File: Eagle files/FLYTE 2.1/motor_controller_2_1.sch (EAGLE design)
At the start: 32 parts, among them J1 XT60-M, U1 MIC29302WU-TRTO-263-5_MCH-M

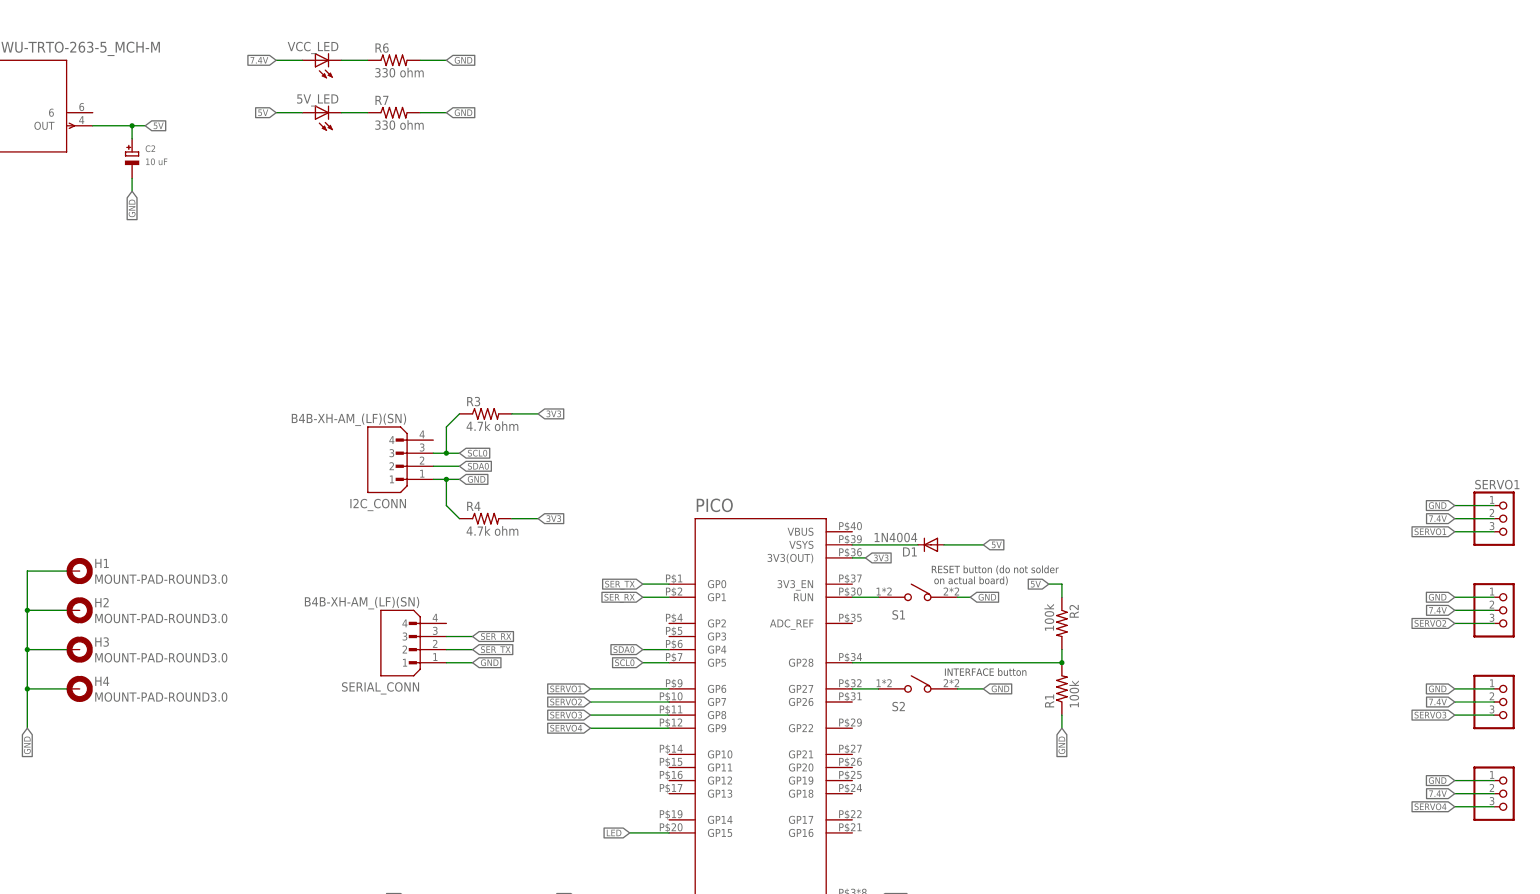
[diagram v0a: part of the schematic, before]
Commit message: Schematics of FC and motor controller
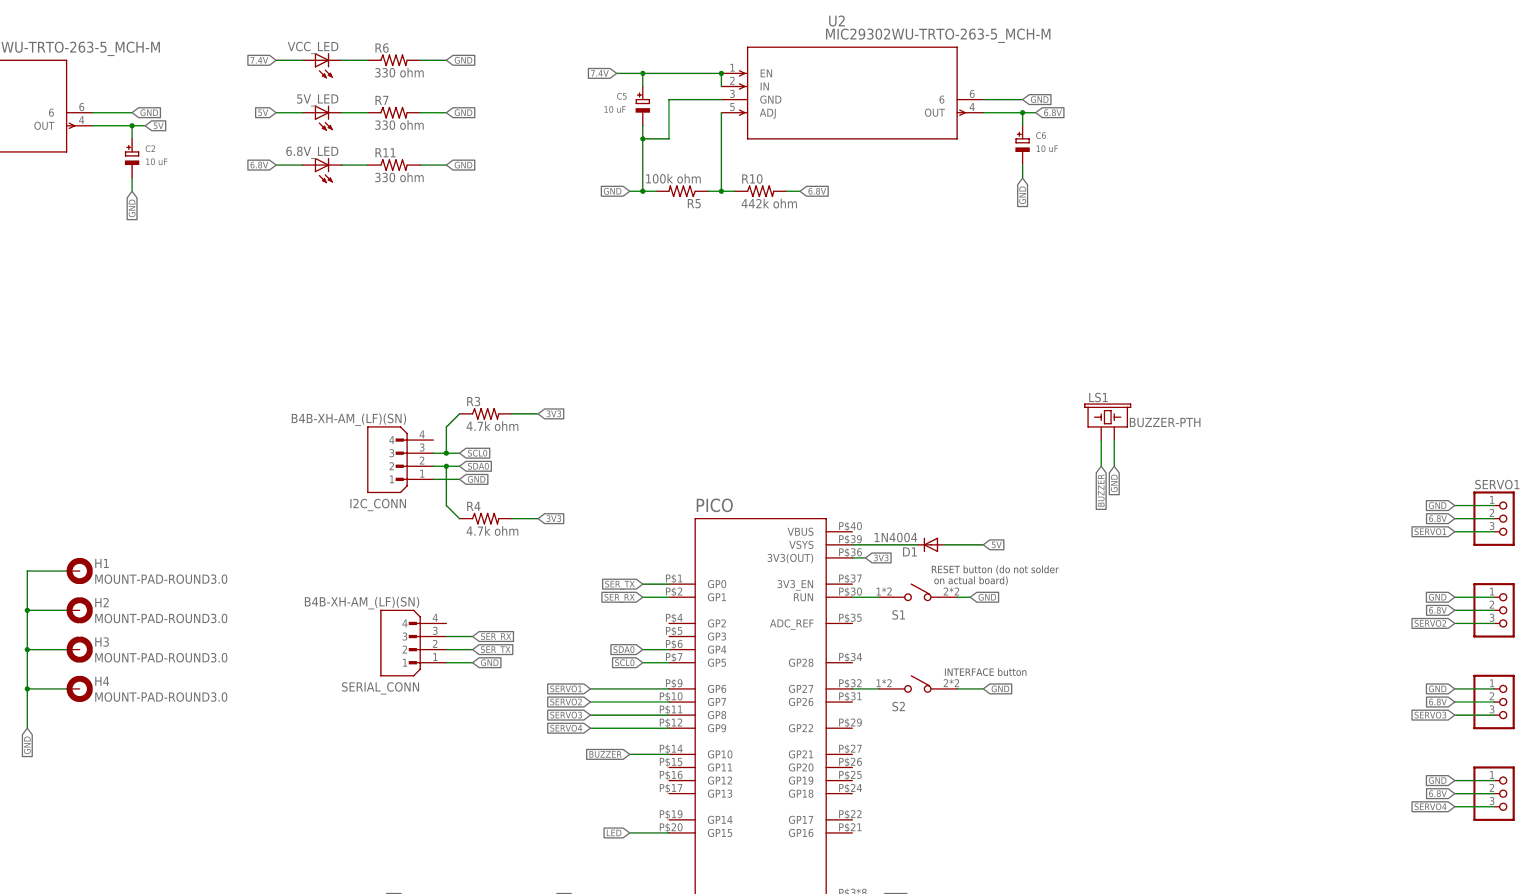
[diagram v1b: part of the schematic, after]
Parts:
- removed R1, R2: 100k, rcl:R-US_R0805
- added 6.8V_LED: (no value), adafruit:LEDCHIPLED_1206
- added C5, C6: 10 uF, microbuilder:CAP_TANTALUMA/3216_WAVE
- added LS1: BUZZER-PTH, SparkFun-Electromechanical:BUZZER-PTH
- added R10: 442k ohm, rcl:R-US_R0805
- added R11: 330 ohm, rcl:R-US_R0805
- added R5: 100k ohm, rcl:R-US_R0805
- added U2: MIC29302WU-TRTO-263-5_MCH-M, MIC29302WU:MIC29302WU-TRTO-263-5_MCH-M
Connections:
- removed net N$4: PICO.GP28, R1.2, R2.2
- new net 6.8V: 6.8V_LED.A, C6.+, R10.2, SERVO1.2, SERVO2.2, SERVO3.2, SERVO4.2, U2.OUT
- new net BUZZER: LS1.1, PICO.GP10
- new net N$5: R10.1, R5.1, U2.ADJ
- new net N$8: 6.8V_LED.C, R11.1
- net 5V: no longer R2.1
- net 7.4V: now also C5.+, U2.EN, U2.IN; no longer SERVO1.2, SERVO2.2, SERVO3.2, SERVO4.2
- net GND: now also C5.-, C6.-, LS1.2, R11.2, R5.2, U1.6, U2.6, U2.GND; no longer R1.1, R4.1
- net SDA0: now also R4.1

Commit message: motor controller v2.1
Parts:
- removed SERVO1, SERVO2, SERVO3, SERVO4: (no value), pinhead:PINHD-1X3
- added J2, J3, J4, J5: S3B-XH-A(LF)(SN), S3B-XH-A_LF__SN_:S3B-XH-A(LF)(SN)
- renumbered S1 to RESET, S2 to INTERFACE
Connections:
- net 6.8V: now also J2.2, J3.2, J4.2, J5.2; no longer SERVO1.2, SERVO2.2, SERVO3.2, SERVO4.2
- net GND: now also J2.1, J3.1, J4.1, J5.1; no longer SERVO1.1, SERVO2.1, SERVO3.1, SERVO4.1
- net SERVO1: now also J2.3; no longer SERVO1.3
- net SERVO2: now also J3.3; no longer SERVO2.3
- net SERVO3: now also J4.3; no longer SERVO3.3
- net SERVO4: now also J5.3; no longer SERVO4.3
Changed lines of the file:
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@@
 <part name="PICO" library="RpiPico" deviceset="RASPBERRY_PICO-NO_DEBUG" device="" override_package3d_urn="urn:adsk.eagle:package:43007819/2" override_package_urn="urn:adsk.eagle:footprint:43007820/1"/>
 <part name="D1" library="adafruit" deviceset="1N4004" device="" override_package3d_urn="urn:adsk.eagle:package:43007855/2" override_package_urn="urn:adsk.eagle:footprint:43007856/1"/>
-<part name="SERVO1" library="pinhead" library_urn="urn:adsk.eagle:library:325" deviceset="PINHD-1X3" device="" package3d_urn="urn:adsk.eagle:package:22458/2"/>
-<part name="SERVO2" library="pinhead" library_urn="urn:adsk.eagle:library:325" deviceset="PINHD-1X3" device="" package3d_urn="urn:adsk.eagle:package:22458/2"/>
-<part name="SERVO3" library="pinhead" library_urn="urn:adsk.eagle:library:325" deviceset="PINHD-1X3" device="" package3d_urn="urn:adsk.eagle:package:22458/2"/>
-<part name="SERVO4" library="pinhead" library_urn="urn:adsk.eagle:library:325" deviceset="PINHD-1X3" device="" package3d_urn="urn:adsk.eagle:package:22458/2"/>
 <part name="H1" library="holes" library_urn="urn:adsk.eagle:library:237" deviceset="MOUNT-PAD-ROUND" device="3.0" package3d_urn="urn:adsk.eagle:package:14280/1" override_package3d_urn="urn:adsk.eagle:package:43007850/2" override_package_urn="urn:adsk.eagle:footprint:14251/1"/>
 <part name="H2" library="holes" library_urn="urn:adsk.eagle:library:237" deviceset="MOUNT-PAD-ROUND" device="3.0" package3d_urn="urn:adsk.eagle:package:14280/1" override_package3d_urn="urn:adsk.eagle:package:43007851/2" override_package_urn="urn:adsk.eagle:footprint:14251/1"/>
@@
 <part name="C3" library="SparkFun-Capacitors" deviceset="22UF" device="-0805-16V-20%" value="22uF"/>
 <part name="C4" library="SparkFun-Capacitors" deviceset="22UF" device="-0805-16V-20%" value="22uF"/>
-<part name="S1" library="TS04-66-95-BK-100-SMT" deviceset="TS04-66-95-BK-100-SMT" device=""/>
-<part name="S2" library="TS04-66-95-BK-100-SMT" deviceset="TS04-66-95-BK-100-SMT" device=""/>
+<part name="RESET" library="TS04-66-95-BK-100-SMT" deviceset="TS04-66-95-BK-100-SMT" device=""/>
+<part name="INTERFACE" library="TS04-66-95-BK-100-SMT" deviceset="TS04-66-95-BK-100-SMT" device=""/>
 <part name="U2" library="MIC29302WU" deviceset="MIC29302WU-TR" device="TO-263-5_MCH-M"/>
 <part name="C5" library="microbuilder" deviceset="CAP_TANTALUM" device="A/3216_WAVE" value="10 uF"/>
@@
 <part name="6.8V_LED" library="adafruit" deviceset="LED" device="CHIPLED_1206"/>
 <part name="R11" library="rcl" library_urn="urn:adsk.eagle:library:334" deviceset="R-US_" device="R0805" package3d_urn="urn:adsk.eagle:package:23553/2" value="330 ohm"/>
+<part name="J2" library="S3B-XH-A_LF__SN_" deviceset="S3B-XH-A(LF)(SN)" device=""/>
+<part name="J3" library="S3B-XH-A_LF__SN_" deviceset="S3B-XH-A(LF)(SN)" device=""/>
+<part name="J4" library="S3B-XH-A_LF__SN_" deviceset="S3B-XH-A(LF)(SN)" device=""/>
+<part name="J5" library="S3B-XH-A_LF__SN_" deviceset="S3B-XH-A(LF)(SN)" device=""/>
 </parts>
 <sheets>
@@
 <attribute name="VALUE" x="248.92" y="147.0914" size="1.778" layer="96" rot="R180"/>
 </instance>
-<instance part="SERVO1" gate="A" x="363.22" y="149.86" smashed="yes">
-<attribute name="NAME" x="356.87" y="155.575" size="1.778" layer="95"/>
-<attribute name="VALUE" x="356.87" y="142.24" size="1.778" layer="96"/>
-</instance>
-<instance part="SERVO2" gate="A" x="363.22" y="132.08" smashed="yes">
-<attribute name="VALUE" x="356.87" y="124.46" size="1.778" layer="96"/>
-</instance>
-<instance part="SERVO3" gate="A" x="363.22" y="114.3" smashed="yes">
-<attribute name="VALUE" x="356.87" y="106.68" size="1.778" layer="96"/>
-</instance>
-<instance part="SERVO4" gate="A" x="363.22" y="96.52" smashed="yes">
-<attribute name="VALUE" x="356.87" y="88.9" size="1.778" layer="96"/>
-</instance>
 <instance part="H1" gate="G$1" x="86.36" y="139.7" smashed="yes">
 <attribute name="NAME" x="89.154" y="140.2842" size="1.778" layer="95"/>
@@
 <attribute name="VALUE" x="194.564" y="66.421" size="1.778" layer="96" font="vector"/>
 </instance>
-<instance part="S1" gate="G$1" x="248.92" y="134.62" smashed="yes">
+<instance part="RESET" gate="G$1" x="248.92" y="134.62" smashed="yes">
 <attribute name="NAME" x="243.84" y="130.302" size="1.778" layer="95"/>
 </instance>
-<instance part="S2" gate="G$1" x="248.92" y="116.84" smashed="yes">
+<instance part="INTERFACE" gate="G$1" x="248.92" y="116.84" smashed="yes">
 <attribute name="NAME" x="243.84" y="112.522" size="1.778" layer="95"/>
 </instance>
@@
 <attribute name="NAME" x="143.51" y="219.9386" size="1.778" layer="95"/>
 <attribute name="VALUE" x="143.51" y="215.138" size="1.778" layer="96"/>
+</instance>
+<instance part="J2" gate="G$1" x="370.84" y="149.86" smashed="yes">
+<attribute name="NAME" x="365.76" y="156.21" size="1.778" layer="95"/>
+<attribute name="VALUE" x="365.76" y="142.24" size="1.778" layer="96"/>
+</instance>
+<instance part="J3" gate="G$1" x="370.84" y="132.08" smashed="yes">
+<attribute name="NAME" x="365.76" y="138.43" size="1.778" layer="95"/>
+<attribute name="VALUE" x="365.76" y="124.46" size="1.778" layer="96"/>
+</instance>
+<instance part="J4" gate="G$1" x="370.84" y="114.3" smashed="yes">
+<attribute name="NAME" x="365.76" y="120.65" size="1.778" layer="95"/>
+<attribute name="VALUE" x="365.76" y="106.68" size="1.778" layer="96"/>
+</instance>
+<instance part="J5" gate="G$1" x="370.84" y="96.52" smashed="yes">
+<attribute name="NAME" x="365.76" y="102.87" size="1.778" layer="95"/>
+<attribute name="VALUE" x="365.76" y="88.9" size="1.778" layer="96"/>
 </instance>
 </instances>
@@
 </segment>
 <segment>
-<pinref part="SERVO1" gate="A" pin="1"/>
 <wire x1="360.68" y1="152.4" x2="353.06" y2="152.4" width="0.1524" layer="91"/>
 <label x="353.06" y="152.4" size="1.27" layer="95" rot="R180" xref="yes"/>
+<pinref part="J2" gate="G$1" pin="1"/>
 </segment>
 <segment>
 <wire x1="360.68" y1="134.62" x2="353.06" y2="134.62" width="0.1524" layer="91"/>
 <label x="353.06" y="134.62" size="1.27" layer="95" rot="R180" xref="yes"/>
-<pinref part="SERVO2" gate="A" pin="1"/>
+<pinref part="J3" gate="G$1" pin="1"/>
 </segment>
 <segment>
 <wire x1="360.68" y1="116.84" x2="353.06" y2="116.84" width="0.1524" layer="91"/>
 <label x="353.06" y="116.84" size="1.27" layer="95" rot="R180" xref="yes"/>
-<pinref part="SERVO3" gate="A" pin="1"/>
+<pinref part="J4" gate="G$1" pin="1"/>
 </segment>
 <segment>
 <wire x1="360.68" y1="99.06" x2="353.06" y2="99.06" width="0.1524" layer="91"/>
 <label x="353.06" y="99.06" size="1.27" layer="95" rot="R180" xref="yes"/>
-<pinref part="SERVO4" gate="A" pin="1"/>
+<pinref part="J5" gate="G$1" pin="1"/>
 </segment>
 <segment>
 <wire x1="256.54" y1="134.62" x2="259.08" y2="134.62" width="0.1524" layer="91"/>
 <label x="259.08" y="134.62" size="1.27" layer="95" xref="yes"/>
-<pinref part="S1" gate="G$1" pin="4"/>
+<pinref part="RESET" gate="G$1" pin="4"/>
 </segment>
 <segment>
 <wire x1="256.54" y1="116.84" x2="261.62" y2="116.84" width="0.1524" layer="91"/>
 <label x="261.62" y="116.84" size="1.27" layer="95" xref="yes"/>
-<pinref part="S2" gate="G$1" pin="4"/>
+<pinref part="INTERFACE" gate="G$1" pin="4"/>
 </segment>
 <segment>
@@
 </segment>
 <segment>
-<pinref part="SERVO1" gate="A" pin="3"/>
 <wire x1="360.68" y1="147.32" x2="353.06" y2="147.32" width="0.1524" layer="91"/>
 <label x="353.06" y="147.32" size="1.27" layer="95" rot="R180" xref="yes"/>
+<pinref part="J2" gate="G$1" pin="3"/>
 </segment>
 </net>
@@
 <wire x1="360.68" y1="129.54" x2="353.06" y2="129.54" width="0.1524" layer="91"/>
 <label x="353.06" y="129.54" size="1.27" layer="95" rot="R180" xref="yes"/>
-<pinref part="SERVO2" gate="A" pin="3"/>
+<pinref part="J3" gate="G$1" pin="3"/>
 </segment>
 </net>
@@
 <wire x1="360.68" y1="111.76" x2="353.06" y2="111.76" width="0.1524" layer="91"/>
 <label x="353.06" y="111.76" size="1.27" layer="95" rot="R180" xref="yes"/>
-<pinref part="SERVO3" gate="A" pin="3"/>
+<pinref part="J4" gate="G$1" pin="3"/>
 </segment>
 </net>
@@
 <wire x1="360.68" y1="93.98" x2="353.06" y2="93.98" width="0.1524" layer="91"/>
 <label x="353.06" y="93.98" size="1.27" layer="95" rot="R180" xref="yes"/>
-<pinref part="SERVO4" gate="A" pin="3"/>
+<pinref part="J5" gate="G$1" pin="3"/>
 </segment>
 </net>
@@
 <segment>
 <pinref part="PICO" gate="G$1" pin="RUN"/>
-<pinref part="S1" gate="G$1" pin="2"/>
+<pinref part="RESET" gate="G$1" pin="2"/>
 <wire x1="236.22" y1="134.62" x2="241.3" y2="134.62" width="0.1524" layer="91"/>
 </segment>
@@
 <segment>
 <pinref part="PICO" gate="G$1" pin="GP27"/>
-<pinref part="S2" gate="G$1" pin="2"/>
+<pinref part="INTERFACE" gate="G$1" pin="2"/>
 <wire x1="236.22" y1="116.84" x2="241.3" y2="116.84" width="0.1524" layer="91"/>
 </segment>
@@
 </segment>
 <segment>
-<pinref part="SERVO1" gate="A" pin="2"/>
 <wire x1="360.68" y1="149.86" x2="353.06" y2="149.86" width="0.1524" layer="91"/>
 <label x="353.06" y="149.86" size="1.27" layer="95" rot="R180" xref="yes"/>
+<pinref part="J2" gate="G$1" pin="2"/>
 </segment>
 <segment>
 <wire x1="360.68" y1="132.08" x2="353.06" y2="132.08" width="0.1524" layer="91"/>
 <label x="353.06" y="132.08" size="1.27" layer="95" rot="R180" xref="yes"/>
-<pinref part="SERVO2" gate="A" pin="2"/>
+<pinref part="J3" gate="G$1" pin="2"/>
 </segment>
 <segment>
 <wire x1="360.68" y1="114.3" x2="353.06" y2="114.3" width="0.1524" layer="91"/>
 <label x="353.06" y="114.3" size="1.27" layer="95" rot="R180" xref="yes"/>
-<pinref part="SERVO3" gate="A" pin="2"/>
+<pinref part="J4" gate="G$1" pin="2"/>
 </segment>
 <segment>
 <wire x1="360.68" y1="96.52" x2="353.06" y2="96.52" width="0.1524" layer="91"/>
 <label x="353.06" y="96.52" size="1.27" layer="95" rot="R180" xref="yes"/>
-<pinref part="SERVO4" gate="A" pin="2"/>
-</segment>
-<segment>
+<pinref part="J5" gate="G$1" pin="2"/>
+</segment>
+<segment>

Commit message: flyte done
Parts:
- 5V_LED, 6.8V_LED, VCC_LED: device adafruit:LEDCHIPLED_1206 -> led:LEDCHIPLED_1206
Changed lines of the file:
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@@
 <part name="GND2" library="52101-101-REV-A_v16" library_urn="urn:adsk.eagle:library:21899384" deviceset="SUPPLY0_GND_" device=""/>
 <part name="GND3" library="52101-101-REV-A_v16" library_urn="urn:adsk.eagle:library:21899384" deviceset="SUPPLY0_GND_" device=""/>
-<part name="J1" library="XT60-M" deviceset="XT60-M" device=""/>
-<part name="SERIAL_CONN" library="B4B-XH-AM__LF__SN_" deviceset="B4B-XH-AM_(LF)(SN)" device=""/>
-<part name="I2C_CONN" library="B4B-XH-AM__LF__SN_" deviceset="B4B-XH-AM_(LF)(SN)" device=""/>
+<part name="J1" library="XT60-M" deviceset="XT60-M" device="" override_package3d_urn="urn:adsk.eagle:package:44253201/2" override_package_urn="urn:adsk.eagle:footprint:44253203/1"/>
+<part name="SERIAL_CONN" library="B4B-XH-AM__LF__SN_" deviceset="B4B-XH-AM_(LF)(SN)" device="" override_package3d_urn="urn:adsk.eagle:package:44253162/2" override_package_urn="urn:adsk.eagle:footprint:44253163/1"/>
+<part name="I2C_CONN" library="B4B-XH-AM__LF__SN_" deviceset="B4B-XH-AM_(LF)(SN)" device="" override_package3d_urn="urn:adsk.eagle:package:44253157/2" override_package_urn="urn:adsk.eagle:footprint:44253158/1"/>
 <part name="R3" library="rcl" library_urn="urn:adsk.eagle:library:334" deviceset="R-US_" device="R0805" package3d_urn="urn:adsk.eagle:package:23553/2" value="4.7k ohm"/>
 <part name="R4" library="rcl" library_urn="urn:adsk.eagle:library:334" deviceset="R-US_" device="R0805" package3d_urn="urn:adsk.eagle:package:23553/2" value="4.7k ohm"/>
-<part name="VCC_LED" library="adafruit" deviceset="LED" device="CHIPLED_1206"/>
-<part name="5V_LED" library="adafruit" deviceset="LED" device="CHIPLED_1206"/>
+<part name="VCC_LED" library="led" library_urn="urn:adsk.eagle:library:259" deviceset="LED" device="CHIPLED_1206" package3d_urn="urn:adsk.eagle:package:15823/2"/>
+<part name="5V_LED" library="led" library_urn="urn:adsk.eagle:library:259" deviceset="LED" device="CHIPLED_1206" package3d_urn="urn:adsk.eagle:package:15823/2"/>
 <part name="R6" library="rcl" library_urn="urn:adsk.eagle:library:334" deviceset="R-US_" device="R0805" package3d_urn="urn:adsk.eagle:package:23553/2" value="330 ohm"/>
 <part name="R7" library="rcl" library_urn="urn:adsk.eagle:library:334" deviceset="R-US_" device="R0805" package3d_urn="urn:adsk.eagle:package:23553/2" value="330 ohm"/>
@@
 <part name="C3" library="SparkFun-Capacitors" deviceset="22UF" device="-0805-16V-20%" value="22uF"/>
 <part name="C4" library="SparkFun-Capacitors" deviceset="22UF" device="-0805-16V-20%" value="22uF"/>
-<part name="RESET" library="TS04-66-95-BK-100-SMT" deviceset="TS04-66-95-BK-100-SMT" device=""/>
-<part name="INTERFACE" library="TS04-66-95-BK-100-SMT" deviceset="TS04-66-95-BK-100-SMT" device=""/>
+<part name="RESET" library="TS04-66-95-BK-100-SMT" deviceset="TS04-66-95-BK-100-SMT" device="" override_package3d_urn="urn:adsk.eagle:package:44253165/2" override_package_urn="urn:adsk.eagle:footprint:44253166/1"/>
+<part name="INTERFACE" library="TS04-66-95-BK-100-SMT" deviceset="TS04-66-95-BK-100-SMT" device="" override_package3d_urn="urn:adsk.eagle:package:44253178/2" override_package_urn="urn:adsk.eagle:footprint:44253179/1"/>
 <part name="U2" library="MIC29302WU" deviceset="MIC29302WU-TR" device="TO-263-5_MCH-M"/>
 <part name="C5" library="microbuilder" deviceset="CAP_TANTALUM" device="A/3216_WAVE" value="10 uF"/>
@@
 <part name="R10" library="rcl" library_urn="urn:adsk.eagle:library:334" deviceset="R-US_" device="R0805" package3d_urn="urn:adsk.eagle:package:23553/2" value="442k ohm"/>
 <part name="LS1" library="SparkFun-Electromechanical" deviceset="BUZZER" device="-PTH"/>
-<part name="6.8V_LED" library="adafruit" deviceset="LED" device="CHIPLED_1206"/>
+<part name="6.8V_LED" library="led" library_urn="urn:adsk.eagle:library:259" deviceset="LED" device="CHIPLED_1206" package3d_urn="urn:adsk.eagle:package:15823/2"/>
 <part name="R11" library="rcl" library_urn="urn:adsk.eagle:library:334" deviceset="R-US_" device="R0805" package3d_urn="urn:adsk.eagle:package:23553/2" value="330 ohm"/>
-<part name="J2" library="S3B-XH-A_LF__SN_" deviceset="S3B-XH-A(LF)(SN)" device=""/>
-<part name="J3" library="S3B-XH-A_LF__SN_" deviceset="S3B-XH-A(LF)(SN)" device=""/>
-<part name="J4" library="S3B-XH-A_LF__SN_" deviceset="S3B-XH-A(LF)(SN)" device=""/>
-<part name="J5" library="S3B-XH-A_LF__SN_" deviceset="S3B-XH-A(LF)(SN)" device=""/>
+<part name="J2" library="S3B-XH-A_LF__SN_" deviceset="S3B-XH-A(LF)(SN)" device="" override_package3d_urn="urn:adsk.eagle:package:44253231/2" override_package_urn="urn:adsk.eagle:footprint:44253232/1"/>
+<part name="J3" library="S3B-XH-A_LF__SN_" deviceset="S3B-XH-A(LF)(SN)" device="" override_package3d_urn="urn:adsk.eagle:package:44253237/2" override_package_urn="urn:adsk.eagle:footprint:44253238/1"/>
+<part name="J4" library="S3B-XH-A_LF__SN_" deviceset="S3B-XH-A(LF)(SN)" device="" override_package3d_urn="urn:adsk.eagle:package:44253239/2" override_package_urn="urn:adsk.eagle:footprint:44253240/1"/>
+<part name="J5" library="S3B-XH-A_LF__SN_" deviceset="S3B-XH-A(LF)(SN)" device="" override_package3d_urn="urn:adsk.eagle:package:44253247/2" override_package_urn="urn:adsk.eagle:footprint:44253248/1"/>
 </parts>
 <sheets>
